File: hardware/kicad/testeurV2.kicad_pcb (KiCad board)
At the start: 2 copper layers, 105 x 65 mm, 35 parts, among them J1 I2C_a, J10 CAN, J2 I2C_b, J3 S1, J4 S2, J5 S3, J6 S4, J7 S5, J8 22-03-5035, J9 22-03-5035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

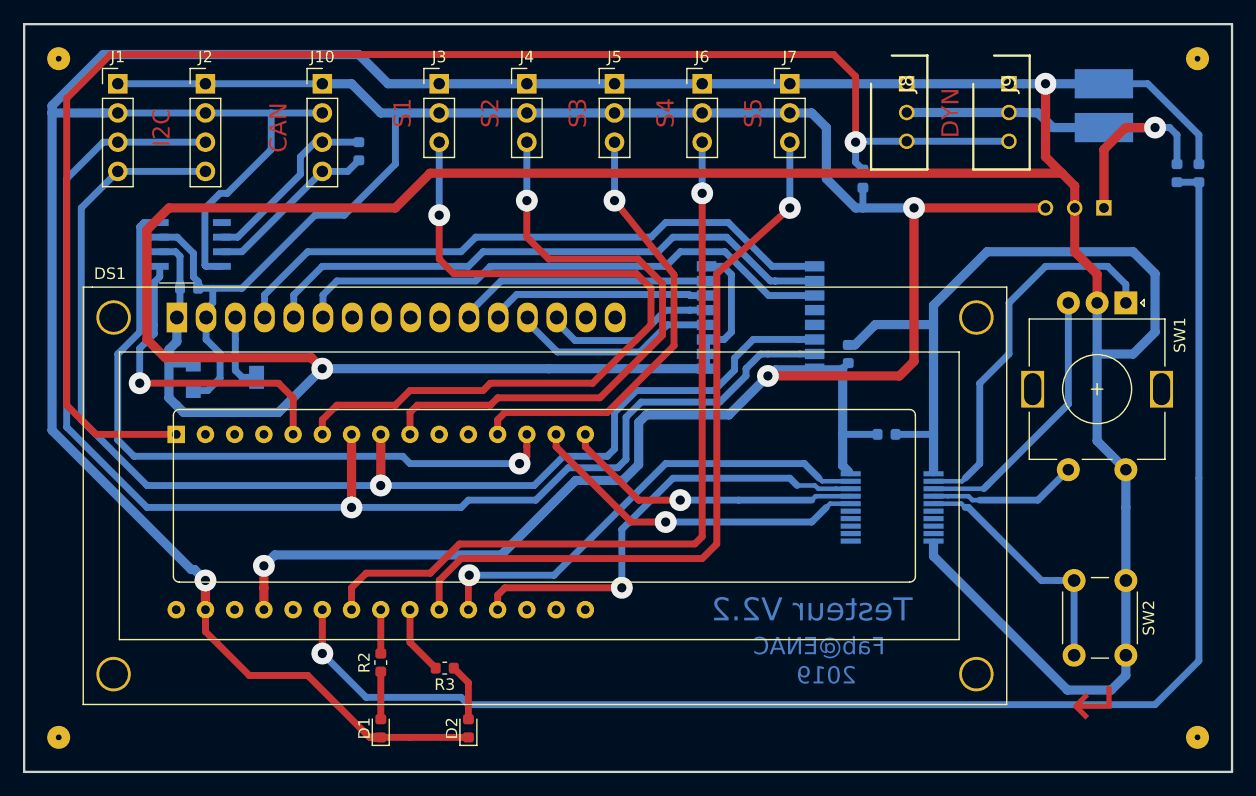
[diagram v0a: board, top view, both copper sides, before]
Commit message: Change directory tree. Adds I2C pullups.
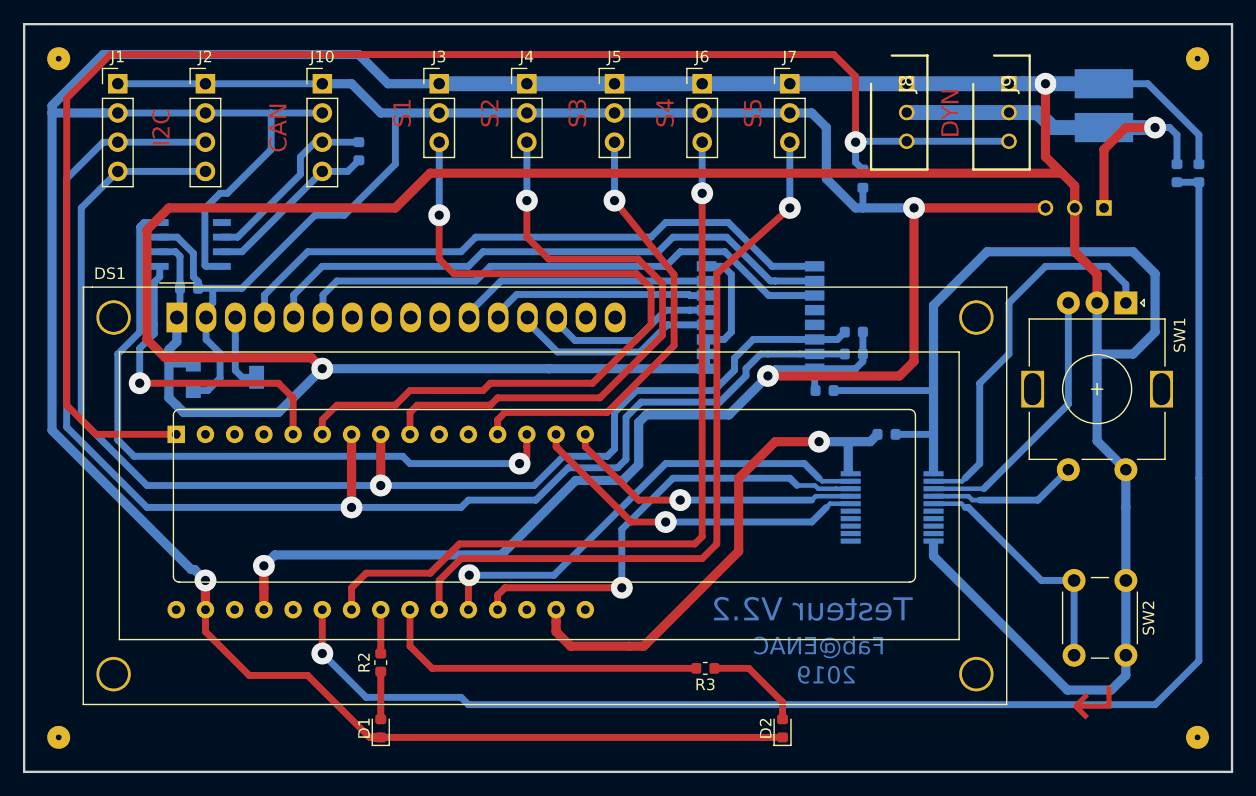
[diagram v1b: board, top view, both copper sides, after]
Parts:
- added R7: 2.2k, Resistor_SMD:R_0603_1608Metric, B.Cu at (168.1, 66.7)
- added R8: 2.2k, Resistor_SMD:R_0603_1608Metric, B.Cu at (168.1, 64.8)
- moved D2 27.3 mm to (161.9, 99.2)
- moved R3 22.7 mm to (155.2, 94.0)
- moved C4 3.78 mm to (165.6, 69.8), turned to 180 degrees
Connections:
- C2 pad 2: +5V -> +3V3
- U3 pad 17: (no net) -> +3V3
- U5 pad 20: +5V -> +3V3
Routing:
- net +3V3: track 0.00 -> 44.3 mm, vias 0 -> 1
- net GND: track 549.8 -> 577.6 mm
- net Net-(R3-Pad2): track 6.01 -> 28.9 mm
- net +5V: track 236.4 -> 230.0 mm
- net Net-(D2-Pad2): track 4.97 -> 8.64 mm
- net /I2C1_SCL: track 108.8 -> 111.7 mm
- net /I2C1_SDA: track 117.3 -> 119.9 mm
